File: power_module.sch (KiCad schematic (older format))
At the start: 17 parts, among them J1 USB_B, J2 CONN_01X02, Q1 Q_NMOS_GSD, U1 ATTINY24A-SSU

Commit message: merged
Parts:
- added J?: CONN_01X04, symbol CONN_01X04
- added J?: CONN_01X05, symbol CONN_01X05
- added R? (x9): R, symbol R
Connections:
- net at U1.13 ((PCINT0/AREF/ADC0)PA0): now also R?.2
- net at U1.2 ((PCINT8/CLKI/XTAL1)PB0): now also R?.2
- net at U1.3 ((PCINT9/XTAL2)PB1): now also R?.2
- net at U1.4 ((PCINT11/dW/~RESET~)PB3): now also R?.2
- net at U1.5 ((PCINT10/CKOUT/OC0A/INT0)PB2): now also R?.2
- net at U1.6 ((PCINT7/ICP/OC0B/ADC7)PA7): now also R?.2
- net at U1.7 ((PCINT6/SDA/DI/MOSI/OC1A/ADC6)PA6): now also R?.2
- net at U1.8 ((PCINT5/DO/MISO/OC1B/ADC5)PA5): now also R?.2
- net at U1.9 ((PCINT4/USCK/SCL/T1/ADC4)PA4): now also R?.2
- new net: J?.1 (P1), R?.1 (x2)
- new net: J?.2 (P2), R?.1 (x2)
- new net: J?.3 (P3), R?.1 (x2)
- new net: J?.4 (P4), R?.1 (x2)
- new net: J?.5 (P5), R?.1
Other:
- moved on the sheet: Q1

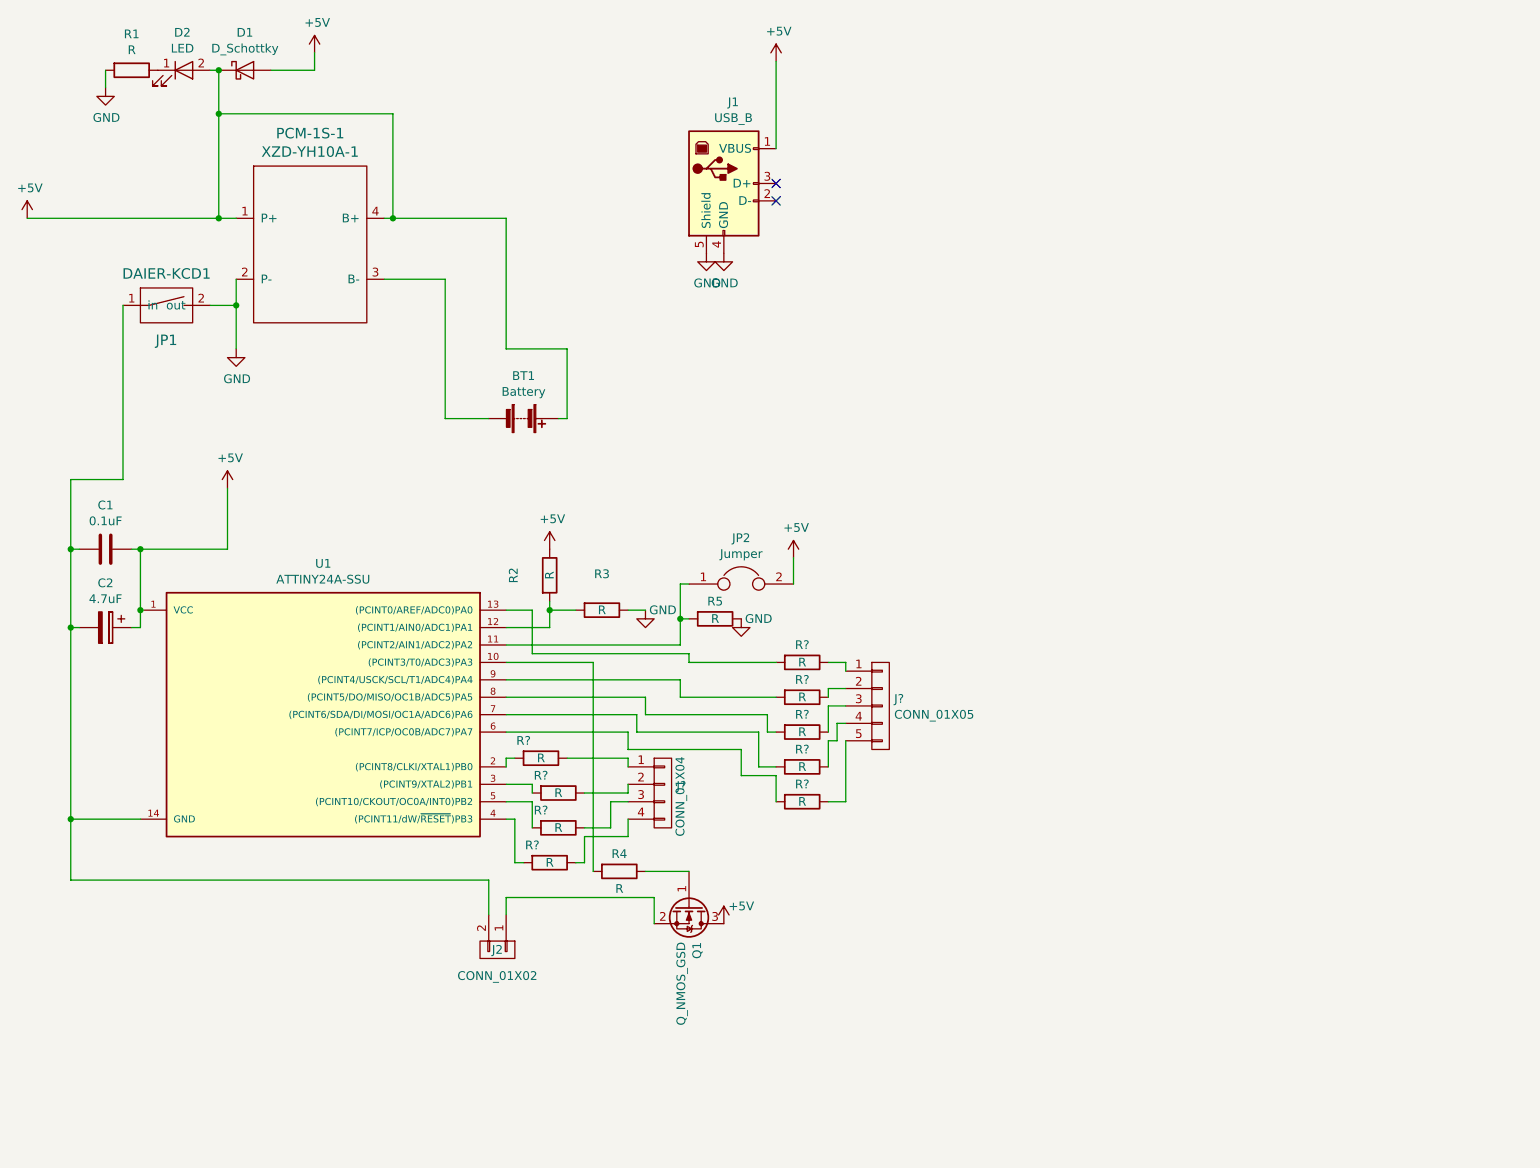
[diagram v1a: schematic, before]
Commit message: add attiny 24-ssu
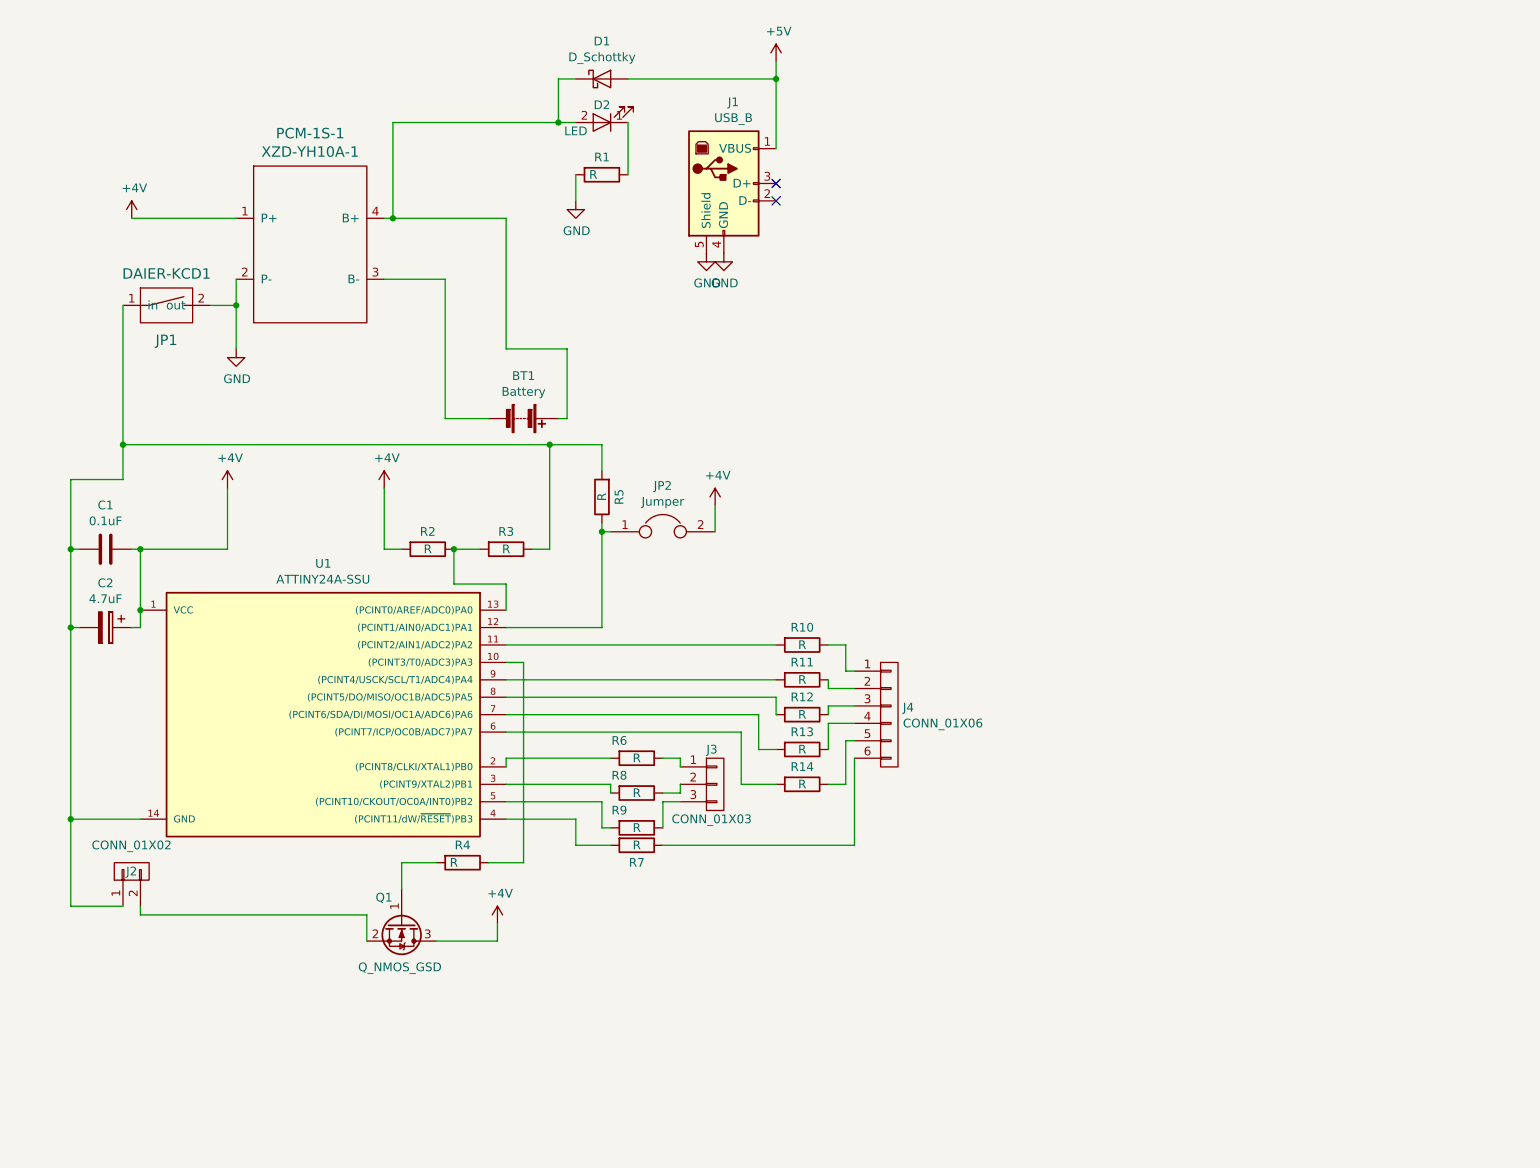
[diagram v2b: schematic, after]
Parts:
- removed J?: CONN_01X04, symbol CONN_01X04
- removed J?: CONN_01X05, symbol CONN_01X05
- added J3: CONN_01X03, Pin_Headers:Pin_Header_Straight_1x03_Pitch2.54mm, symbol CONN_01X03
- added J4: CONN_01X06, Pin_Headers:Pin_Header_Straight_1x06_Pitch2.54mm, symbol CONN_01X06
- C1: footprint (none) -> Capacitors_SMD:C_0603
- C2: footprint (none) -> Capacitors_Tantalum_SMD:CP_Tantalum_Case-D_EIA-7343-31_Reflow
- D2: footprint (none) -> LEDs:LED_D3.0mm_Horizontal_O3.81mm_Z6.0mm
- JP2: footprint (none) -> Pin_Headers:Pin_Header_Straight_1x02_Pitch2.54mm
- Q1: footprint (none) -> TO_SOT_Packages_SMD:SOT-23
- R1, R2, R3, R4, R5: footprint (none) -> Resistors_SMD:R_1206
- R10, R11, R12, R13, R14, R6, R7, R8, R9: renamed from R?; footprint (none) -> Resistors_SMD:R_1206
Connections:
- net +5V: no longer BT1.1 (+), C1.1, C2.1, D1.1 (K), D2.2 (A), JP2.2, PCM-1S-1.1 (P+), PCM-1S-1.4 (B+), Q1.3 (D), R2.1, U1.1 (VCC)
- net GND: no longer R3.1, R5.1
- net at J2.1 (P1): now also C1.2, C2.2, JP1.1 (in), R3.1, R5.2, U1.14 (GND); no longer Q1.2 (S)
- net at U1.10 ((PCINT3/T0/ADC3)PA3): now also R4.1; no longer R4.2
- net at R10.2: now also U1.11 ((PCINT2/AIN1/ADC2)PA2); no longer U1.13 ((PCINT0/AREF/ADC0)PA0)
- net at R10.1: now also J4.1 (P1)
- net at R6.1: now also J3.1 (P1)
- net at R8.1: now also J3.2 (P2)
- net at R9.1: now also J3.3 (P3)
- net at R7.1: now also J4.6 (P6)
- net at Q1.1 (G): now also R4.2; no longer R4.1
- net at R11.1: now also J4.2 (P2)
- net at R12.1: now also J4.3 (P3)
- net at R13.1: now also J4.4 (P4)
- net at R14.1: now also J4.5 (P5)
- new net: BT1.1 (+), D1.1 (K), D2.2 (A), PCM-1S-1.4 (B+)
- new net: J2.2 (P2), Q1.2 (S)
- new net: JP2.1, R5.1, U1.12 ((PCINT1/AIN0/ADC1)PA1)
- new net: R2.1, R3.2, U1.13 ((PCINT0/AREF/ADC0)PA0)
- new net +4V: C1.1, C2.1, JP2.2, PCM-1S-1.1 (P+), Q1.3 (D), R2.2, U1.1 (VCC)
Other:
- moved on the sheet: D1, D2, J2, JP2, Q1, R1, R10, R11, R12, R13, R14, R2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

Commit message: Correct pcb
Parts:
- added R15: 47K, Resistors_SMD:R_1206, symbol R
- C1: footprint Capacitors_SMD:C_0603 -> Capacitors_SMD:C_0805
- J2: value CONN_01X02 -> VOUT
- R1, R3: value R -> 330
- R2: value R -> 1.5K
- R4: value R -> 0
- R5: value R -> 47K
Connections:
- net +5V: now also D2.2 (A)
- net at BT1.1 (+), D1.1 (K), PCM-1S-1.4 (B+): no longer D2.2 (A)
- net GNDA: now reaches C1.2, C2.2, J2.1 (P1), JP1.1 (in), R3.1, R5.2, U1.14 (GND)
- net GNDA: now also R15.2
- net at U1.10 ((PCINT3/T0/ADC3)PA3): now also R4.2; no longer R4.1
- net ss: now reaches R14.2, U1.6 ((PCINT7/ICP/OC0B/ADC7)PA7)
- net mosi: now reaches R13.2, U1.7 ((PCINT6/SDA/DI/MOSI/OC1A/ADC6)PA6)
- net miso: now reaches R12.2, U1.8 ((PCINT5/DO/MISO/OC1B/ADC5)PA5)
- net sck: now reaches R11.2, U1.9 ((PCINT4/USCK/SCL/T1/ADC4)PA4)
- net at Q1.1 (G): now also R4.1, R15.1; no longer R4.2
- net reset: now reaches J4.6 (P6), R7.1
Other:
- moved on the sheet: D1, J2, Q1, R4, R5
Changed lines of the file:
@@
 L CONN_01X02 J2
 U 1 1 595F9E1D
-P 2000 6150
-F 0 "J2" V 2000 6150 50  0000 C CNN
-F 1 "CONN_01X02" V 2150 6150 50  0000 C CNN
-F 2 "Pin_Headers:Pin_Header_Angled_1x02_Pitch2.54mm" H 2000 6150 50  0001 C CNN
-F 3 "" H 2000 6150 50  0001 C CNN
-	1    2000 6150
-	0    -1   -1   0
+P 4450 7050
+F 0 "J2" V 4450 7050 50  0000 C CNN
+F 1 "VOUT" V 4600 7050 50  0000 C CNN
+F 2 "Pin_Headers:Pin_Header_Angled_1x02_Pitch2.54mm" H 4450 7050 50  0001 C CNN
+F 3 "" H 4450 7050 50  0001 C CNN
+	1    4450 7050
+	-1   0    0    1
 $EndComp
 $Comp
@@
 L D_Schottky D1
 U 1 1 595FC216
-P 4700 1600
-F 0 "D1" H 4700 1816 50  0000 C CNN
-F 1 "D_Schottky" H 4700 1725 50  0000 C CNN
-F 2 "Diodes_THT:D_DO-201AD_P15.24mm_Horizontal" H 4700 1600 50  0001 C CNN
-F 3 "" H 4700 1600 50  0001 C CNN
-	1    4700 1600
+P 4000 1850
+F 0 "D1" H 4000 2066 50  0000 C CNN
+F 1 "D_Schottky" H 4000 1975 50  0000 C CNN
+F 2 "Diodes_THT:D_DO-201AD_P15.24mm_Horizontal" H 4000 1850 50  0001 C CNN
+F 3 "" H 4000 1850 50  0001 C CNN
+	1    4000 1850
 	1    0    0    -1
 $EndComp
@@
 P 4700 2150
 F 0 "R1" V 4600 2150 50  0000 C CNN
-F 1 "R" V 4700 2100 50  0000 C CNN
+F 1 "330" V 4700 2150 50  0000 C CNN
 F 2 "Resistors_SMD:R_1206" V 4630 2150 50  0001 C CNN
 F 3 "" H 4700 2150 50  0001 C CNN
@@
 F 0 "C1" V 1598 4300 50  0000 C CNN
 F 1 "0.1uF" V 1689 4300 50  0000 C CNN
-F 2 "Capacitors_SMD:C_0603" H 1888 4150 50  0001 C CNN
+F 2 "Capacitors_SMD:C_0805" H 1888 4150 50  0001 C CNN
 F 3 "" H 1850 4300 50  0001 C CNN
 	1    1850 4300
@@
 P 3700 4300
 F 0 "R2" V 3600 4300 50  0000 C CNN
-F 1 "R" V 3700 4300 50  0000 C CNN
+F 1 "1.5K" V 3700 4300 50  0000 C CNN
 F 2 "Resistors_SMD:R_1206" V 3630 4300 50  0001 C CNN
 F 3 "" H 3700 4300 50  0001 C CNN
@@
 P 4150 4300
 F 0 "R3" V 4050 4300 50  0000 C CNN
-F 1 "R" V 4150 4300 50  0000 C CNN
+F 1 "330" V 4150 4300 50  0000 C CNN
 F 2 "Resistors_SMD:R_1206" V 4080 4300 50  0001 C CNN
 F 3 "" H 4150 4300 50  0001 C CNN
@@
 L R R5
 U 1 1 5980B68F
-P 4700 4000
-F 0 "R5" V 4600 4000 50  0000 C CNN
-F 1 "R" V 4700 4000 50  0000 C CNN
-F 2 "Resistors_SMD:R_1206" V 4630 4000 50  0001 C CNN
-F 3 "" H 4700 4000 50  0001 C CNN
-	1    4700 4000
-	-1   0    0    1
+P 5050 4450
+F 0 "R5" V 4950 4450 50  0000 C CNN
+F 1 "47K" V 5050 4450 50  0000 C CNN
+F 2 "Resistors_SMD:R_1206" V 4980 4450 50  0001 C CNN
+F 3 "" H 5050 4450 50  0001 C CNN
+	1    5050 4450
+	0    -1   -1   0
 $EndComp
 $Comp
 L Q_NMOS_GSD Q1
 U 1 1 5980B948
-P 3550 6450
-F 0 "Q1" V 3400 6300 50  0000 L CNN
-F 1 "Q_NMOS_GSD" V 3800 6200 50  0000 L CNN
-F 2 "TO_SOT_Packages_SMD:SOT-23" H 3750 6550 50  0001 C CNN
-F 3 "" H 3550 6450 50  0001 C CNN
-	1    3550 6450
-	0    1    1    0
+P 4600 6550
+F 0 "Q1" V 4450 6400 50  0000 L CNN
+F 1 "Q_NMOS_GSD" V 4850 6300 50  0000 L CNN
+F 2 "TO_SOT_Packages_SMD:SOT-23" H 4800 6650 50  0001 C CNN
+F 3 "" H 4600 6550 50  0001 C CNN
+	1    4600 6550
+	1    0    0    -1
 $EndComp
 $Comp
 L R R4
 U 1 1 5980C6FE
-P 3900 6100
-F 0 "R4" V 3800 6100 50  0000 C CNN
-F 1 "R" V 3900 6050 50  0000 C CNN
-F 2 "Resistors_SMD:R_1206" V 3830 6100 50  0001 C CNN
-F 3 "" H 3900 6100 50  0001 C CNN
-	1    3900 6100
-	0    1    1    0
+P 4350 6200
+F 0 "R4" V 4250 6200 50  0000 C CNN
+F 1 "0" V 4350 6150 50  0000 C CNN
+F 2 "Resistors_SMD:R_1206" V 4280 6200 50  0001 C CNN
+F 3 "" H 4350 6200 50  0001 C CNN
+	1    4350 6200
+	-1   0    0    1
 $EndComp
 $Comp
@@
 L +4V #PWR010
 U 1 1 5982CA37
-P 4100 6450
-F 0 "#PWR010" H 4100 6300 50  0001 C CNN
-F 1 "+4V" H 4115 6623 50  0000 C CNN
-F 2 "" H 4100 6450 50  0001 C CNN
-F 3 "" H 4100 6450 50  0001 C CNN
-	1    4100 6450
+P 4700 6300
+F 0 "#PWR010" H 4700 6150 50  0001 C CNN
+F 1 "+4V" H 4715 6473 50  0000 C CNN
+F 2 "" H 4700 6300 50  0001 C CNN
+F 3 "" H 4700 6300 50  0001 C CNN
+	1    4700 6300
 	1    0    0    -1
 $EndComp
@@
 Connection ~ 3850 4300
 Wire Wire Line
-	4300 4300 4400 4300
+	4300 4300 4500 4300
 Wire Wire Line
 	5350 4200 5350 4050
@@
 Connection ~ 1650 5850
 Wire Wire Line
-	1650 3900 1650 6350
+	1650 3900 1650 6700
 Wire Wire Line
 	4150 5250 5600 5250
@@
 	5500 5350 5500 5650
 Wire Wire Line
-	3350 6400 3350 6550
-Wire Wire Line
-	4850 1600 5700 1600
+	4450 1600 5700 1600
 Connection ~ 5700 1600
-Wire Wire Line
-	3500 1850 4550 1850
 Connection ~ 4450 1850
 Wire Wire Line
@@
 	4850 2150 4850 1850
 Wire Wire Line
-	4550 1600 4450 1600
-Wire Wire Line
 	4450 1600 4450 1850
 Wire Wire Line
@@
 	5050 5750 5150 5750
 Wire Wire Line
-	1650 6350 1950 6350
-Wire Wire Line
-	3550 6250 3550 6100
-Wire Wire Line
-	3550 6100 3750 6100
-Wire Wire Line
 	5050 5700 5150 5700
 Wire Wire Line
@@
 	4750 5650 4750 5700
 Wire Wire Line
-	4050 6100 4250 6100
-Wire Wire Line
-	4250 6100 4250 4950
-Wire Wire Line
-	4250 4950 4150 4950
-Wire Wire Line
-	3750 6550 4100 6550
-Wire Wire Line
-	4100 6550 4100 6450
+	4150 4950 4350 4950
 Wire Wire Line
 	5050 6000 6150 6000
@@
 Wire Wire Line
 	4550 6000 4750 6000
-Wire Wire Line
-	4400 4300 4400 3700
-Wire Wire Line
-	1950 3700 4700 3700
 Connection ~ 1950 3700
-Wire Wire Line
-	4700 4150 4700 4750
-Connection ~ 4700 4200
-Wire Wire Line
-	4700 3700 4700 3850
-Connection ~ 4400 3700
-Wire Wire Line
-	2050 6350 2050 6400
-Wire Wire Line
-	2050 6400 3350 6400
 $Comp
 L CONN_01X06 J4
@@
 	1    0    0    -1
 $EndComp
+Wire Wire Line
+	4350 4950 4350 6050
+Wire Wire Line
+	4350 6350 4350 6550
+Wire Wire Line
+	4350 6550 4400 6550
+Wire Wire Line
+	4700 6300 4700 6350
+$Comp
+L R R15
+U 1 1 59837FC6
+P 4100 6700
+F 0 "R15" H 4170 6746 50  0000 L CNN
+F 1 "47K" H 4170 6655 50  0000 L CNN
+F 2 "Resistors_SMD:R_1206" V 4030 6700 50  0001 C CNN
+F 3 "" H 4100 6700 50  0001 C CNN
+	1    4100 6700
+	1    0    0    -1
+$EndComp
+Wire Wire Line
+	4350 6400 4100 6400
+Connection ~ 4350 6400
+$Comp
+L GNDA #PWR011
+U 1 1 598388C3
+P 4700 7300
+F 0 "#PWR011" H 4700 7050 50  0001 C CNN
+F 1 "GNDA" H 4705 7127 50  0000 C CNN
+F 2 "" H 4700 7300 50  0001 C CNN
+F 3 "" H 4700 7300 50  0001 C CNN
+	1    4700 7300
+	1    0    0    -1
+$EndComp
+$Comp
+L GNDA #PWR012
+U 1 1 5983901B
+P 4100 6950
+F 0 "#PWR012" H 4100 6700 50  0001 C CNN
+F 1 "GNDA" H 4105 6777 50  0000 C CNN
+F 2 "" H 4100 6950 50  0001 C CNN
+F 3 "" H 4100 6950 50  0001 C CNN
+	1    4100 6950
+	1    0    0    -1
+$EndComp
+Wire Wire Line
+	4100 6850 4100 6950
+Wire Wire Line
+	4100 6400 4100 6550
+Wire Wire Line
+	3500 1850 3850 1850
+Wire Wire Line
+	4150 1850 4550 1850
+$Comp
+L GNDA #PWR013
+U 1 1 5983AD8B
+P 4500 4400
+F 0 "#PWR013" H 4500 4150 50  0001 C CNN
+F 1 "GNDA" H 4505 4227 50  0000 C CNN
+F 2 "" H 4500 4400 50  0001 C CNN
+F 3 "" H 4500 4400 50  0001 C CNN
+	1    4500 4400
+	1    0    0    -1
+$EndComp
+$Comp
+L GNDA #PWR014
+U 1 1 5983B405
+P 5400 4550
+F 0 "#PWR014" H 5400 4300 50  0001 C CNN
+F 1 "GNDA" H 5405 4377 50  0000 C CNN
+F 2 "" H 5400 4550 50  0001 C CNN
+F 3 "" H 5400 4550 50  0001 C CNN
+	1    5400 4550
+	1    0    0    -1
+$EndComp
+Wire Wire Line
+	4700 4200 4700 4750
+Wire Wire Line
+	4700 4450 4900 4450
+Wire Wire Line
+	5200 4450 5400 4450
+Wire Wire Line
+	5400 4450 5400 4550
+Connection ~ 4700 4450
+Wire Wire Line
+	4500 4300 4500 4400
+Wire Wire Line
+	4700 6750 4700 7000
+$Comp
+L GNDA #PWR015
+U 1 1 5983E4C7
+P 1650 6700
+F 0 "#PWR015" H 1650 6450 50  0001 C CNN
+F 1 "GNDA" H 1655 6527 50  0000 C CNN
+F 2 "" H 1650 6700 50  0001 C CNN
+F 3 "" H 1650 6700 50  0001 C CNN
+	1    1650 6700
+	1    0    0    -1
+$EndComp
+Wire Wire Line
+	4700 7000 4650 7000
+Wire Wire Line
+	4650 7100 4700 7100
+Wire Wire Line
+	4700 7100 4700 7300
+Text Label 4650 5250 0    60   ~ 0
+mosi
+Text Label 4650 5150 0    60   ~ 0
+miso
+Text Label 4700 5050 0    60   ~ 0
+sck
+Text Label 5850 6000 0    60   ~ 0
+reset
+Text Label 4750 5350 0    60   ~ 0
+ss
 $EndSCHEMATC
